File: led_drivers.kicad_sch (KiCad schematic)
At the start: 7 parts, among them IC1 SamacSys_Parts_HT16K33-28SOP, IC2 SamacSys_Parts_HT16K33-28SOP

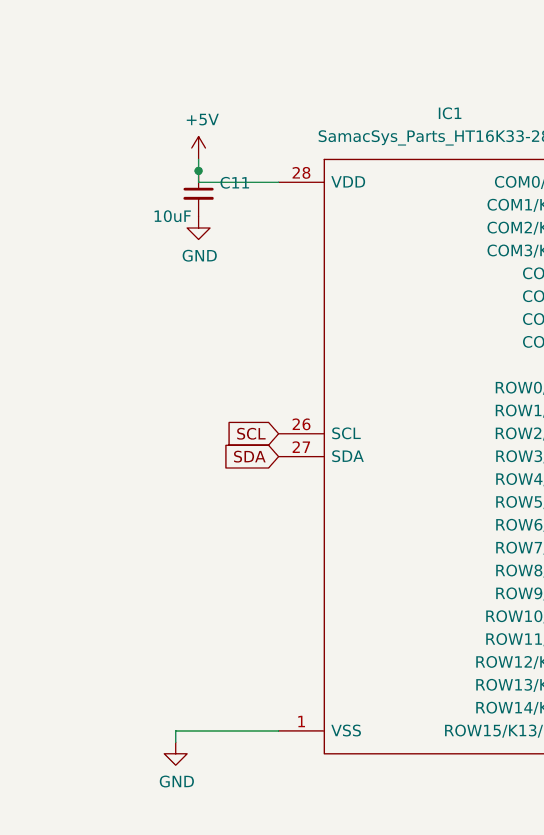
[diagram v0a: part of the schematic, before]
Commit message: Add testpoints
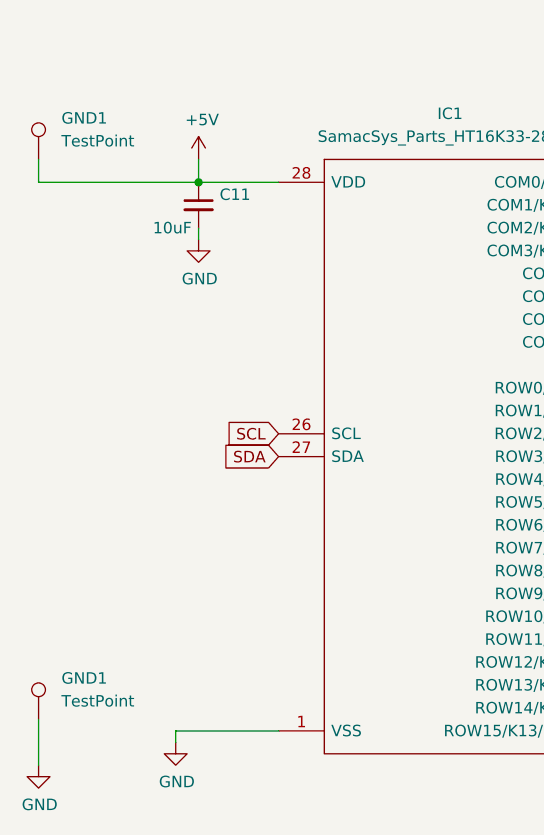
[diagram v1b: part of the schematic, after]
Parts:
- added GND1 (x2): TestPoint, TestPoint:TestPoint_Pad_D1.0mm, symbol Connector:TestPoint
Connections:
- net +5V: now also GND1.1
- net GND: now also GND1.1
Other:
- moved on the sheet: C11
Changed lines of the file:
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@@
   (junction (at 190.5 52.07) (diameter 0) (color 0 0 0 0)
   )
+  (junction (at 45.72 53.34) (diameter 0) (color 0 0 0 0)
+  )
   (junction (at 147.32 48.26) (diameter 0) (color 0 0 0 0)
   )
   (junction (at 152.4 52.07) (diameter 0) (color 0 0 0 0)
-  )
-  (junction (at 45.72 52.07) (diameter 0) (color 0 0 0 0)
   )
   (no_connect (at 193.04 69.85))
@@
     (stroke (width 0) (type default))
   )
+  (wire (pts (xy 45.72 50.8) (xy 45.72 53.34))
+    (stroke (width 0) (type default))
+  )
   (wire (pts (xy 190.5 97.79) (xy 193.04 97.79))
     (stroke (width 0) (type default))
@@
     (stroke (width 0) (type default))
   )
+  (wire (pts (xy 27.94 113.03) (xy 27.94 118.11))
+    (stroke (width 0) (type default))
+  )
   (wire (pts (xy 151.13 63.5) (xy 147.32 63.5))
     (stroke (width 0) (type default))
@@
     (stroke (width 0) (type default))
   )
+  (wire (pts (xy 45.72 53.34) (xy 27.94 53.34))
+    (stroke (width 0) (type default))
+  )
+  (wire (pts (xy 45.72 58.42) (xy 45.72 59.69))
+    (stroke (width 0) (type default))
+  )
   (wire (pts (xy 190.5 82.55) (xy 193.04 82.55))
     (stroke (width 0) (type default))
@@
     (stroke (width 0) (type default))
   )
-  (wire (pts (xy 45.72 52.07) (xy 45.72 50.8))
-    (stroke (width 0) (type default))
-  )
   (wire (pts (xy 190.5 102.87) (xy 193.04 102.87))
     (stroke (width 0) (type default))
@@
     (stroke (width 0) (type default))
   )
+  (wire (pts (xy 27.94 50.8) (xy 27.94 53.34))
+    (stroke (width 0) (type default))
+  )
   (wire (pts (xy 152.4 52.07) (xy 152.4 48.26))
     (stroke (width 0) (type default))
@@
   )
   (wire (pts (xy 190.5 90.17) (xy 193.04 90.17))
-    (stroke (width 0) (type default))
-  )
-  (wire (pts (xy 45.72 53.34) (xy 45.72 52.07))
     (stroke (width 0) (type default))
   )
@@
     )
   )
-  (symbol (lib_id "Device:C_Small") (at 45.72 54.61 0) (unit 1)
+  (symbol (lib_id "power:GND") (at 27.94 118.11 0) (unit 1)
     (in_bom yes) (on_board yes) (dnp no)
-    (property "Reference" "C11" (at 48.0568 53.4416 0)
+    (property "Reference" "#PWR029" (at 27.94 124.46 0)
+      (effects (font (size 1.27 1.27)) hide)
+    )
+    (property "Value" "GND" (at 28.067 122.5042 0)
+      (effects (font (size 1.27 1.27)))
+    )
+    (property "Footprint" "" (at 27.94 118.11 0)
+      (effects (font (size 1.27 1.27)) hide)
+    )
+    (property "Datasheet" "" (at 27.94 118.11 0)
+      (effects (font (size 1.27 1.27)) hide)
+    )
+    (pin "1")
+    (instances
+      (project "LTP305_ESP32_CLOCK"
+        (path "/c007e288-8439-49d9-bbdf-49724c34958c"
+          (reference "#PWR029") (unit 1)
+        )
+      )
+      (project "ltp_kikad"
+        (path "/eed35b77-cbf9-4596-9b17-2558f81058ba/2fb8f433-d537-4253-8cc8-f6d42368ed9e"
+          (reference "#PWR037") (unit 1)
+        )
+        (path "/eed35b77-cbf9-4596-9b17-2558f81058ba/7d22e16e-a0ba-4766-b1de-c8cbb28f14f7"
+          (reference "#PWR069") (unit 1)
+        )
+      )
+    )
+  )
+  (symbol (lib_id "Device:C_Small") (at 45.72 55.88 0) (unit 1)
+    (in_bom yes) (on_board yes) (dnp no)
+    (property "Reference" "C11" (at 48.0568 54.7116 0)
       (effects (font (size 1.27 1.27)) (justify left))
     )
-    (property "Value" "10uF" (at 40.64 57.15 0)
+    (property "Value" "10uF" (at 40.64 58.42 0)
       (effects (font (size 1.27 1.27)) (justify left))
     )
-    (property "Footprint" "Capacitor_SMD:C_0603_1608Metric" (at 45.72 54.61 0)
-      (effects (font (size 1.27 1.27)) hide)
-    )
-    (property "Datasheet" "~" (at 45.72 54.61 0)
+    (property "Footprint" "Capacitor_SMD:C_0603_1608Metric" (at 45.72 55.88 0)
+      (effects (font (size 1.27 1.27)) hide)
+    )
+    (property "Datasheet" "~" (at 45.72 55.88 0)
       (effects (font (size 1.27 1.27)) hide)
     )
@@
         (path "/eed35b77-cbf9-4596-9b17-2558f81058ba/7d22e16e-a0ba-4766-b1de-c8cbb28f14f7"
           (reference "C1") (unit 1)
+        )
+      )
+    )
+  )
+  (symbol (lib_id "Connector:TestPoint") (at 27.94 113.03 0) (unit 1)
+    (in_bom yes) (on_board yes) (dnp no) (fields_autoplaced)
+    (property "Reference" "GND1" (at 30.48 108.458 0)
+      (effects (font (size 1.27 1.27)) (justify left))
+    )
+    (property "Value" "TestPoint" (at 30.48 110.998 0)
+      (effects (font (size 1.27 1.27)) (justify left))
+    )
+    (property "Footprint" "TestPoint:TestPoint_Pad_D1.0mm" (at 33.02 113.03 0)
+      (effects (font (size 1.27 1.27)) hide)
+    )
+    (property "Datasheet" "~" (at 33.02 113.03 0)
+      (effects (font (size 1.27 1.27)) hide)
+    )
+    (pin "1")
+    (instances
+      (project "ltp_kikad"
+        (path "/eed35b77-cbf9-4596-9b17-2558f81058ba/2fb8f433-d537-4253-8cc8-f6d42368ed9e"
+          (reference "GND1") (unit 1)
+        )
+        (path "/eed35b77-cbf9-4596-9b17-2558f81058ba/7d22e16e-a0ba-4766-b1de-c8cbb28f14f7"
+          (reference "GND2") (unit 1)
+        )
+      )
+    )
+  )
+  (symbol (lib_id "Connector:TestPoint") (at 27.94 50.8 0) (unit 1)
+    (in_bom yes) (on_board yes) (dnp no) (fields_autoplaced)
+    (property "Reference" "GND1" (at 30.48 46.228 0)
+      (effects (font (size 1.27 1.27)) (justify left))
+    )
+    (property "Value" "TestPoint" (at 30.48 48.768 0)
+      (effects (font (size 1.27 1.27)) (justify left))
+    )
+    (property "Footprint" "TestPoint:TestPoint_Pad_D1.0mm" (at 33.02 50.8 0)
+      (effects (font (size 1.27 1.27)) hide)
+    )
+    (property "Datasheet" "~" (at 33.02 50.8 0)
+      (effects (font (size 1.27 1.27)) hide)
+    )
+    (pin "1")
+    (instances
+      (project "ltp_kikad"
+        (path "/eed35b77-cbf9-4596-9b17-2558f81058ba/2fb8f433-d537-4253-8cc8-f6d42368ed9e"
+          (reference "GND1") (unit 1)
+        )
+        (path "/eed35b77-cbf9-4596-9b17-2558f81058ba/7d22e16e-a0ba-4766-b1de-c8cbb28f14f7"
+          (reference "+5v1") (unit 1)
         )
       )
@@
     )
   )
-  (symbol (lib_id "power:GND") (at 45.72 57.15 0) (unit 1)
+  (symbol (lib_id "power:GND") (at 45.72 59.69 0) (unit 1)
     (in_bom yes) (on_board yes) (dnp no)
-    (property "Reference" "#PWR038" (at 45.72 63.5 0)
-      (effects (font (size 1.27 1.27)) hide)
-    )
-    (property "Value" "GND" (at 45.847 61.5442 0)
+    (property "Reference" "#PWR038" (at 45.72 66.04 0)
+      (effects (font (size 1.27 1.27)) hide)
+    )
+    (property "Value" "GND" (at 45.847 64.0842 0)
       (effects (font (size 1.27 1.27)))
     )
-    (property "Footprint" "" (at 45.72 57.15 0)
-      (effects (font (size 1.27 1.27)) hide)
-    )
-    (property "Datasheet" "" (at 45.72 57.15 0)
-      (effects (font (size 1.27 1.27)) hide)
-    )
+    (property "Footprint" "" (at 45.72 59.69 0)
+      (effects (font (size 1.27 1.27)) hide)
+    )
+    (property "Datasheet" "" (at 45.72 59.69 0)
+      (effects (font (size 1.27 1.27)) hide)
+    )

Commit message: Updates silkscreen
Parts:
- removed C11: 10uF, Capacitor_SMD:C_0603_1608Metric, symbol Device:C_Small
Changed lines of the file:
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@@
   (junction (at 147.32 48.26) (diameter 0) (color 0 0 0 0)
-  )
-  (junction (at 152.4 52.07) (diameter 0) (color 0 0 0 0)
   )
   (no_connect (at 193.04 69.85))
@@
     (stroke (width 0) (type default))
   )
-  (wire (pts (xy 147.32 68.58) (xy 147.32 71.12))
-    (stroke (width 0) (type default))
-  )
   (wire (pts (xy 190.5 74.93) (xy 193.04 74.93))
     (stroke (width 0) (type default))
@@
     (stroke (width 0) (type default))
   )
-  (wire (pts (xy 151.13 52.07) (xy 151.13 63.5))
-    (stroke (width 0) (type default))
-  )
   (wire (pts (xy 92.71 88.9) (xy 97.79 88.9))
     (stroke (width 0) (type default))
@@
     (stroke (width 0) (type default))
   )
-  (wire (pts (xy 151.13 63.5) (xy 147.32 63.5))
-    (stroke (width 0) (type default))
-  )
   (wire (pts (xy 92.71 106.68) (xy 97.79 106.68))
     (stroke (width 0) (type default))
@@
   )
   (wire (pts (xy 190.5 107.95) (xy 193.04 107.95))
-    (stroke (width 0) (type default))
-  )
-  (wire (pts (xy 151.13 52.07) (xy 152.4 52.07))
     (stroke (width 0) (type default))
   )
@@
     )
   )
-  (symbol (lib_id "power:GND") (at 147.32 71.12 0) (unit 1)
-    (in_bom yes) (on_board yes) (dnp no)
-    (property "Reference" "#PWR038" (at 147.32 77.47 0)
-      (effects (font (size 1.27 1.27)) hide)
-    )
-    (property "Value" "GND" (at 147.447 75.5142 0)
-      (effects (font (size 1.27 1.27)))
-    )
-    (property "Footprint" "" (at 147.32 71.12 0)
-      (effects (font (size 1.27 1.27)) hide)
-    )
-    (property "Datasheet" "" (at 147.32 71.12 0)
-      (effects (font (size 1.27 1.27)) hide)
-    )
-    (pin "1")
-    (instances
-      (project "LTP305_ESP32_CLOCK"
-        (path "/c007e288-8439-49d9-bbdf-49724c34958c"
-          (reference "#PWR038") (unit 1)
-        )
-      )
-      (project "ltp_kikad"
-        (path "/eed35b77-cbf9-4596-9b17-2558f81058ba"
-          (reference "#PWR012") (unit 1)
-        )
-        (path "/eed35b77-cbf9-4596-9b17-2558f81058ba/7d22e16e-a0ba-4766-b1de-c8cbb28f14f7"
-          (reference "#PWR06") (unit 1)
-        )
-      )
-    )
-  )
   (symbol (lib_id "Device:D") (at 194.31 41.91 180) (unit 1)
     (in_bom yes) (on_board yes) (dnp no)
@@
         )
       )
-    )
-  )
-  (symbol (lib_id "Device:C_Small") (at 147.32 66.04 0) (unit 1)
-    (in_bom yes) (on_board yes) (dnp no)
-    (property "Reference" "C11" (at 149.6568 64.8716 0)
-      (effects (font (size 1.27 1.27)) (justify left))
-    )
-    (property "Value" "10uF" (at 142.24 68.58 0)
-      (effects (font (size 1.27 1.27)) (justify left))
-    )
-    (property "Footprint" "Capacitor_SMD:C_0603_1608Metric" (at 147.32 66.04 0)
-      (effects (font (size 1.27 1.27)) hide)
-    )
-    (property "Datasheet" "~" (at 147.32 66.04 0)
-      (effects (font (size 1.27 1.27)) hide)
-    )
-    (pin "1")
-    (pin "2")
-    (instances
-      (project "LTP305_ESP32_CLOCK"
-        (path "/c007e288-8439-49d9-bbdf-49724c34958c"
-          (reference "C11") (unit 1)
-        )
-      )
-      (project "ltp_kikad"
-        (path "/eed35b77-cbf9-4596-9b17-2558f81058ba"
-          (reference "C7") (unit 1)
-        )
-        (path "/eed35b77-cbf9-4596-9b17-2558f81058ba/7d22e16e-a0ba-4766-b1de-c8cbb28f14f7"
-          (reference "C7") (unit 1)
-        )
-      )

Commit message: Fix connections
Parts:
- removed GND1 (x2): TestPoint, TestPoint:TestPoint_Pad_D1.0mm, symbol Connector:TestPoint
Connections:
- no-connect marks 2 -> 4
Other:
- moved on the sheet: C11
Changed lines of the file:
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@@
   (junction (at 45.72 53.34) (diameter 0) (color 0 0 0 0)
   )
-  (junction (at 147.32 48.26) (diameter 0) (color 0 0 0 0)
-  )
+  (junction (at 140.97 52.07) (diameter 0) (color 0 0 0 0)
+  )
+  (no_connect (at 93.98 71.12))
+  (no_connect (at 95.25 114.3))
   (no_connect (at 193.04 69.85))
   (no_connect (at 193.04 113.03))
+  (wire (pts (xy 140.97 49.53) (xy 140.97 52.07))
+    (stroke (width 0) (type default))
+  )
   (wire (pts (xy 190.5 77.47) (xy 193.04 77.47))
     (stroke (width 0) (type default))
@@
     (stroke (width 0) (type default))
   )
-  (wire (pts (xy 152.4 48.26) (xy 147.32 48.26))
-    (stroke (width 0) (type default))
-  )
-  (wire (pts (xy 27.94 113.03) (xy 27.94 118.11))
+  (wire (pts (xy 152.4 52.07) (xy 140.97 52.07))
     (stroke (width 0) (type default))
   )
@@
     (stroke (width 0) (type default))
   )
-  (wire (pts (xy 45.72 53.34) (xy 27.94 53.34))
-    (stroke (width 0) (type default))
-  )
   (wire (pts (xy 45.72 58.42) (xy 45.72 59.69))
     (stroke (width 0) (type default))
@@
     (stroke (width 0) (type default))
   )
-  (wire (pts (xy 27.94 50.8) (xy 27.94 53.34))
-    (stroke (width 0) (type default))
-  )
-  (wire (pts (xy 152.4 52.07) (xy 152.4 48.26))
-    (stroke (width 0) (type default))
-  )
   (wire (pts (xy 92.71 58.42) (xy 96.52 58.42))
     (stroke (width 0) (type default))
@@
     (stroke (width 0) (type default))
   )
-  (wire (pts (xy 147.32 49.53) (xy 147.32 48.26))
+  (wire (pts (xy 140.97 53.34) (xy 140.97 52.07))
     (stroke (width 0) (type default))
   )
@@
     )
   )
-  (symbol (lib_id "Device:C_Small") (at 147.32 52.07 0) (unit 1)
-    (in_bom yes) (on_board yes) (dnp no)
-    (property "Reference" "C11" (at 149.6568 50.9016 0)
+  (symbol (lib_id "Device:C_Small") (at 140.97 55.88 0) (unit 1)
+    (in_bom yes) (on_board yes) (dnp no)
+    (property "Reference" "C11" (at 143.3068 54.7116 0)
       (effects (font (size 1.27 1.27)) (justify left))
     )
-    (property "Value" "10uF" (at 142.24 54.61 0)
+    (property "Value" "10uF" (at 135.89 58.42 0)
       (effects (font (size 1.27 1.27)) (justify left))
     )
-    (property "Footprint" "Capacitor_SMD:C_0603_1608Metric" (at 147.32 52.07 0)
-      (effects (font (size 1.27 1.27)) hide)
-    )
-    (property "Datasheet" "~" (at 147.32 52.07 0)
+    (property "Footprint" "Capacitor_SMD:C_0603_1608Metric" (at 140.97 55.88 0)
+      (effects (font (size 1.27 1.27)) hide)
+    )
+    (property "Datasheet" "~" (at 140.97 55.88 0)
       (effects (font (size 1.27 1.27)) hide)
     )
@@
     )
   )
-  (symbol (lib_id "power:GND") (at 27.94 118.11 0) (unit 1)
-    (in_bom yes) (on_board yes) (dnp no)
-    (property "Reference" "#PWR029" (at 27.94 124.46 0)
-      (effects (font (size 1.27 1.27)) hide)
-    )
-    (property "Value" "GND" (at 28.067 122.5042 0)
-      (effects (font (size 1.27 1.27)))
-    )
-    (property "Footprint" "" (at 27.94 118.11 0)
-      (effects (font (size 1.27 1.27)) hide)
-    )
-    (property "Datasheet" "" (at 27.94 118.11 0)
-      (effects (font (size 1.27 1.27)) hide)
-    )
-    (pin "1")
-    (instances
-      (project "LTP305_ESP32_CLOCK"
-        (path "/c007e288-8439-49d9-bbdf-49724c34958c"
-          (reference "#PWR029") (unit 1)
-        )
-      )
-      (project "ltp_kikad"
-        (path "/eed35b77-cbf9-4596-9b17-2558f81058ba/2fb8f433-d537-4253-8cc8-f6d42368ed9e"
-          (reference "#PWR037") (unit 1)
-        )
-        (path "/eed35b77-cbf9-4596-9b17-2558f81058ba/7d22e16e-a0ba-4766-b1de-c8cbb28f14f7"
-          (reference "#PWR069") (unit 1)
-        )
-      )
-    )
-  )
   (symbol (lib_id "Device:C_Small") (at 45.72 55.88 0) (unit 1)
     (in_bom yes) (on_board yes) (dnp no)
@@
         (path "/eed35b77-cbf9-4596-9b17-2558f81058ba/7d22e16e-a0ba-4766-b1de-c8cbb28f14f7"
           (reference "C1") (unit 1)
-        )
-      )
-    )
-  )
-  (symbol (lib_id "Connector:TestPoint") (at 27.94 113.03 0) (unit 1)
-    (in_bom yes) (on_board yes) (dnp no) (fields_autoplaced)
-    (property "Reference" "GND1" (at 30.48 108.458 0)
-      (effects (font (size 1.27 1.27)) (justify left))
-    )
-    (property "Value" "TestPoint" (at 30.48 110.998 0)
-      (effects (font (size 1.27 1.27)) (justify left))
-    )
-    (property "Footprint" "TestPoint:TestPoint_Pad_D1.0mm" (at 33.02 113.03 0)
-      (effects (font (size 1.27 1.27)) hide)
-    )
-    (property "Datasheet" "~" (at 33.02 113.03 0)
-      (effects (font (size 1.27 1.27)) hide)
-    )
-    (pin "1")
-    (instances
-      (project "ltp_kikad"
-        (path "/eed35b77-cbf9-4596-9b17-2558f81058ba/2fb8f433-d537-4253-8cc8-f6d42368ed9e"
-          (reference "GND1") (unit 1)
-        )
-        (path "/eed35b77-cbf9-4596-9b17-2558f81058ba/7d22e16e-a0ba-4766-b1de-c8cbb28f14f7"
-          (reference "GND2") (unit 1)
-        )
-      )
-    )
-  )
-  (symbol (lib_id "Connector:TestPoint") (at 27.94 50.8 0) (unit 1)
-    (in_bom yes) (on_board yes) (dnp no) (fields_autoplaced)
-    (property "Reference" "GND1" (at 30.48 46.228 0)
-      (effects (font (size 1.27 1.27)) (justify left))
-    )
-    (property "Value" "TestPoint" (at 30.48 48.768 0)
-      (effects (font (size 1.27 1.27)) (justify left))
-    )
-    (property "Footprint" "TestPoint:TestPoint_Pad_D1.0mm" (at 33.02 50.8 0)
-      (effects (font (size 1.27 1.27)) hide)
-    )
-    (property "Datasheet" "~" (at 33.02 50.8 0)
-      (effects (font (size 1.27 1.27)) hide)
-    )
-    (pin "1")
-    (instances
-      (project "ltp_kikad"
-        (path "/eed35b77-cbf9-4596-9b17-2558f81058ba/2fb8f433-d537-4253-8cc8-f6d42368ed9e"
-          (reference "GND1") (unit 1)
-        )
-        (path "/eed35b77-cbf9-4596-9b17-2558f81058ba/7d22e16e-a0ba-4766-b1de-c8cbb28f14f7"
-          (reference "+5v1") (unit 1)
         )
       )
@@
     )
   )
-  (symbol (lib_id "power:GND") (at 147.32 54.61 0) (unit 1)
-    (in_bom yes) (on_board yes) (dnp no)
-    (property "Reference" "#PWR038" (at 147.32 60.96 0)
-      (effects (font (size 1.27 1.27)) hide)
-    )
-    (property "Value" "GND" (at 147.447 59.0042 0)
-      (effects (font (size 1.27 1.27)))
-    )
-    (property "Footprint" "" (at 147.32 54.61 0)
-      (effects (font (size 1.27 1.27)) hide)
-    )
-    (property "Datasheet" "" (at 147.32 54.61 0)
+  (symbol (lib_id "power:GND") (at 140.97 58.42 0) (unit 1)
+    (in_bom yes) (on_board yes) (dnp no)
+    (property "Reference" "#PWR038" (at 140.97 64.77 0)
+      (effects (font (size 1.27 1.27)) hide)
+    )
+    (property "Value" "GND" (at 141.097 62.8142 0)
+      (effects (font (size 1.27 1.27)))
+    )
+    (property "Footprint" "" (at 140.97 58.42 0)
+      (effects (font (size 1.27 1.27)) hide)
+    )
+    (property "Datasheet" "" (at 140.97 58.42 0)
       (effects (font (size 1.27 1.27)) hide)
     )
@@
     )
   )
-  (symbol (lib_id "power:+5V") (at 147.32 48.26 0) (unit 1)
-    (in_bom yes) (on_board yes) (dnp no)
-    (property "Reference" "#PWR08" (at 147.32 52.07 0)
-      (effects (font (size 1.27 1.27)) hide)
-    )
-    (property "Value" "+5V" (at 147.701 43.8658 0)
-      (effects (font (size 1.27 1.27)))
-    )
-    (property "Footprint" "" (at 147.32 48.26 0)
-      (effects (font (size 1.27 1.27)) hide)
-    )
-    (property "Datasheet" "" (at 147.32 48.26 0)
-      (effects (font (size 1.27 1.27)) hide)
-    )
+  (symbol (lib_id "power:+5V") (at 140.97 49.53 0) (unit 1)
+    (in_bom yes) (on_board yes) (dnp no)
+    (property "Reference" "#PWR08" (at 140.97 53.34 0)
+      (effects (font (size 1.27 1.27)) hide)
+    )
+    (property "Value" "+5V" (at 141.351 45.1358 0)
+      (effects (font (size 1.27 1.27)))
+    )
+    (property "Footprint" "" (at 140.97 49.53 0)
+      (effects (font (size 1.27 1.27)) hide)
+    )
+    (property "Datasheet" "" (at 140.97 49.53 0)
+      (effects (font (size 1.27 1.27)) hide)
+    )
